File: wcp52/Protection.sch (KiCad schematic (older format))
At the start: 14 parts

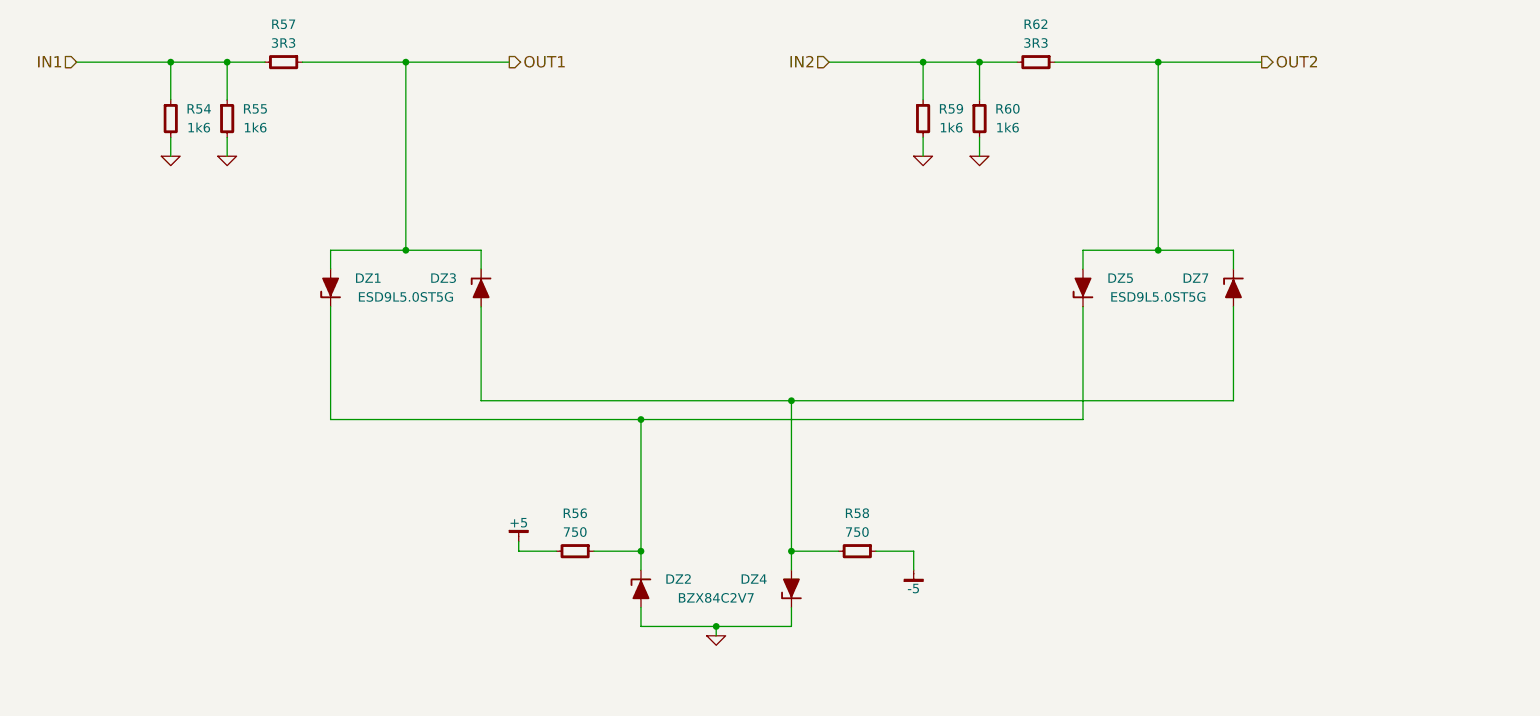
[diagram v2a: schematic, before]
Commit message: Reannotate parts. May need to tweak silkscreen
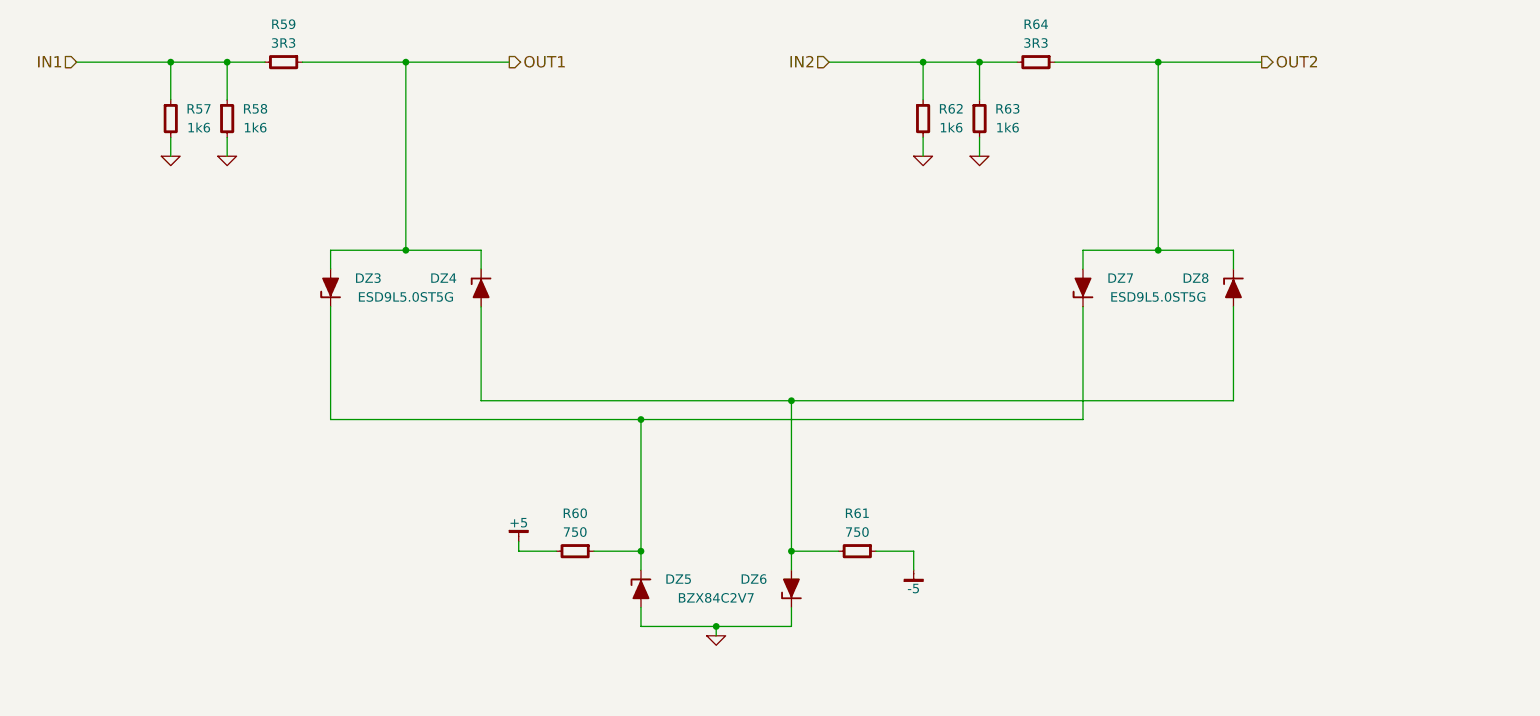
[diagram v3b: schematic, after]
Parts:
- DZ3: renamed from DZ1; OldReference (none) -> DZ1
- DZ4: renamed from DZ3; OldReference (none) -> DZ3
- DZ5: renamed from DZ2; OldReference (none) -> DZ2
- DZ6: renamed from DZ4; OldReference (none) -> DZ4
- DZ7: renamed from DZ5; OldReference (none) -> DZ5
- DZ8: renamed from DZ7; OldReference (none) -> DZ7
- R57: renamed from R54; OldReference (none) -> R54
- R58: renamed from R55; OldReference (none) -> R55
- R59: renamed from R57; OldReference (none) -> R57
- R60: renamed from R56; OldReference (none) -> R56
- R61: renamed from R58; OldReference (none) -> R58
- R62: renamed from R59; OldReference (none) -> R59
- R63: renamed from R60; OldReference (none) -> R60
- R64: renamed from R62; OldReference (none) -> R62
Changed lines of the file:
@@
 F 2 "" H 2900 2800 60  0000 C CNN
 F 3 "" H 2900 2800 60  0000 C CNN
+F 4 "#PWR0171" H 2900 2800 50  0001 C CNN "OldReference"
 	1    2900 2800
 	1    0    0    -1
@@
 F 2 "" H 3200 2800 60  0000 C CNN
 F 3 "" H 3200 2800 60  0000 C CNN
+F 4 "#PWR0172" H 3200 2800 50  0001 C CNN "OldReference"
 	1    3200 2800
 	1    0    0    -1
@@
 Connection ~ 3200 2300
 $Comp
-L ESD9L DZ1
+L ESD9L DZ3
 U 1 1 54F315E0
 P 3750 3500
-F 0 "DZ1" H 3950 3450 50  0000 C CNN
+F 0 "DZ3" H 3950 3450 50  0000 C CNN
 F 1 "ESD9L5.0ST5G" H 4150 3550 50  0000 C CNN
 F 2 "smd-semi:SOD-923" H 3750 3500 50  0001 C CNN
@@
 F 4 "Value" H 3750 3500 60  0001 C CNN "Manuf"
 F 5 "DIST DIGIKEY ESD9L5.0ST5GOSCT-ND" H 3750 3500 60  0001 C CNN "BOM"
+F 6 "DZ1" H 3750 3500 50  0001 C CNN "OldReference"
 	1    3750 3500
 	1    0    0    1
 $EndComp
 $Comp
-L ESD9L DZ3
+L ESD9L DZ4
 U 1 1 54F316A8
 P 4550 3500
-F 0 "DZ3" H 4350 3550 50  0000 C CNN
+F 0 "DZ4" H 4350 3550 50  0000 C CNN
 F 1 "ESD9L5.0ST5G" H 4950 3550 50  0001 C CNN
 F 2 "smd-semi:SOD-923" H 4550 3500 50  0001 C CNN
@@
 F 5 "ONSemi" H 4550 3500 60  0001 C CNN "Manuf"
 F 6 "DIST DIGIKEY ESD9L5.0ST5GOSCT-ND" H 4550 3500 60  0001 C CNN "BOM"
+F 7 "DZ3" H 4550 3500 50  0001 C CNN "OldReference"
 	1    4550 3500
 	1    0    0    -1
 $EndComp
 $Comp
-L BZX84 DZ2
+L BZX84 DZ5
 U 1 1 54F319D0
 P 5400 5100
-F 0 "DZ2" H 5600 5150 50  0000 C CNN
+F 0 "DZ5" H 5600 5150 50  0000 C CNN
 F 1 "BZX84C2V7" H 5800 5050 50  0000 C CNN
 F 2 "smd-semi:SOT-23" H 5400 5100 50  0001 C CNN
@@
 F 5 "ONSemi" H 5400 5100 60  0001 C CNN "Manuf"
 F 6 "DIST DIGIKEY BZX84C2V7LT1GOSCT-ND" H 5400 5100 60  0001 C CNN "BOM"
+F 7 "DZ2" H 5400 5100 50  0001 C CNN "OldReference"
 	1    5400 5100
 	1    0    0    -1
 $EndComp
 $Comp
-L BZX84 DZ4
+L BZX84 DZ6
 U 1 1 54F321AA
 P 6200 5100
-F 0 "DZ4" H 6000 5050 50  0000 C CNN
+F 0 "DZ6" H 6000 5050 50  0000 C CNN
 F 1 "BZX84C2V7" H 6600 5050 50  0001 C CNN
 F 2 "smd-semi:SOT-23" H 6200 5100 50  0001 C CNN
@@
 F 5 "ONSemi" H 6200 5100 60  0001 C CNN "Manuf"
 F 6 "DIST DIGIKEY BZX84C2V7LT1GOSCT-ND" H 6200 5100 60  0001 C CNN "BOM"
+F 7 "DZ4" H 6200 5100 50  0001 C CNN "OldReference"
 	1    6200 5100
 	1    0    0    1
@@
 F 2 "" H 5800 5350 60  0000 C CNN
 F 3 "" H 5800 5350 60  0000 C CNN
+F 4 "#PWR0173" H 5800 5350 50  0001 C CNN "OldReference"
 	1    5800 5350
 	1    0    0    -1
@@
 F 2 "" H 4750 4850 60  0000 C CNN
 F 3 "" H 4750 4850 60  0000 C CNN
+F 4 "#PWR0174" H 4750 4850 50  0001 C CNN "OldReference"
 	1    4750 4850
 	1    0    0    -1
@@
 F 2 "" H 6850 5000 60  0000 C CNN
 F 3 "" H 6850 5000 60  0000 C CNN
+F 4 "#PWR0175" H 6850 5000 50  0001 C CNN "OldReference"
 	1    6850 5000
 	1    0    0    -1
@@
 F 2 "" H 6900 2800 60  0000 C CNN
 F 3 "" H 6900 2800 60  0000 C CNN
+F 4 "#PWR0176" H 6900 2800 50  0001 C CNN "OldReference"
 	1    6900 2800
 	1    0    0    -1
@@
 F 2 "" H 7200 2800 60  0000 C CNN
 F 3 "" H 7200 2800 60  0000 C CNN
+F 4 "#PWR0177" H 7200 2800 50  0001 C CNN "OldReference"
 	1    7200 2800
 	1    0    0    -1
@@
 Connection ~ 7200 2300
 $Comp
-L ESD9L DZ5
+L ESD9L DZ7
 U 1 1 54F32C26
 P 7750 3500
-F 0 "DZ5" H 7950 3450 50  0000 C CNN
+F 0 "DZ7" H 7950 3450 50  0000 C CNN
 F 1 "ESD9L5.0ST5G" H 8150 3550 50  0000 C CNN
 F 2 "smd-semi:SOD-923" H 7750 3500 50  0001 C CNN
@@
 F 4 "Value" H 7750 3500 60  0001 C CNN "Manuf"
 F 5 "DIST DIGIKEY ESD9L5.0ST5GOSCT-ND" H 7750 3500 60  0001 C CNN "BOM"
+F 6 "DZ5" H 7750 3500 50  0001 C CNN "OldReference"
 	1    7750 3500
 	1    0    0    1
 $EndComp
 $Comp
-L ESD9L DZ7
+L ESD9L DZ8
 U 1 1 54F32C2F
 P 8550 3500
-F 0 "DZ7" H 8350 3550 50  0000 C CNN
+F 0 "DZ8" H 8350 3550 50  0000 C CNN
 F 1 "ESD9L5.0ST5G" H 8950 3550 50  0001 C CNN
 F 2 "smd-semi:SOD-923" H 8550 3500 50  0001 C CNN
@@
 F 5 "ONSemi" H 8550 3500 60  0001 C CNN "Manuf"
 F 6 "DIST DIGIKEY ESD9L5.0ST5GOSCT-ND" H 8550 3500 60  0001 C CNN "BOM"
+F 7 "DZ7" H 8550 3500 50  0001 C CNN "OldReference"
 	1    8550 3500
 	1    0    0    -1
@@
 Connection ~ 6200 4100
 $Comp
-L R-0603 R54
+L R-0603 R57
 U 1 1 5503F4A5
 P 2900 2600
-F 0 "R54" H 3050 2650 50  0000 C CNN
+F 0 "R57" H 3050 2650 50  0000 C CNN
 F 1 "1k6" H 3050 2550 50  0000 C CNN
 F 2 "IPC7351-Nominal:RESC1608X50" H 2900 2600 50  0001 C CNN
@@
 F 4 "Value" H 2900 2600 60  0001 C CNN "Manuf"
 F 5 "RES SMD 1.6k 1% [0603]" H 3650 3150 60  0001 C CNN "BOM"
+F 6 "R54" H 2900 2600 50  0001 C CNN "OldReference"
 	1    2900 2600
 	1    0    0    -1
 $EndComp
 $Comp
-L R-0603 R55
+L R-0603 R58
 U 1 1 5503F6C4
 P 3200 2600
-F 0 "R55" H 3350 2650 50  0000 C CNN
+F 0 "R58" H 3350 2650 50  0000 C CNN
 F 1 "1k6" H 3350 2550 50  0000 C CNN
 F 2 "IPC7351-Nominal:RESC1608X50" H 3200 2600 50  0001 C CNN
@@
 F 4 "Value" H 3200 2600 60  0001 C CNN "Manuf"
 F 5 "RES SMD 1.6k 1% [0603]" H 3950 3150 60  0001 C CNN "BOM"
+F 6 "R55" H 3200 2600 50  0001 C CNN "OldReference"
 	1    3200 2600
 	1    0    0    -1
 $EndComp
 $Comp
-L R-0603 R59
+L R-0603 R62
 U 1 1 5503F702
 P 6900 2600
-F 0 "R59" H 7050 2650 50  0000 C CNN
+F 0 "R62" H 7050 2650 50  0000 C CNN
 F 1 "1k6" H 7050 2550 50  0000 C CNN
 F 2 "IPC7351-Nominal:RESC1608X50" H 6900 2600 50  0001 C CNN
@@
 F 4 "Value" H 6900 2600 60  0001 C CNN "Manuf"
 F 5 "RES SMD 1.6k 1% [0603]" H 7650 3150 60  0001 C CNN "BOM"
+F 6 "R59" H 6900 2600 50  0001 C CNN "OldReference"
 	1    6900 2600
 	1    0    0    -1
 $EndComp
 $Comp
-L R-0603 R60
+L R-0603 R63
 U 1 1 5503F89E
 P 7200 2600
-F 0 "R60" H 7350 2650 50  0000 C CNN
+F 0 "R63" H 7350 2650 50  0000 C CNN
 F 1 "1k6" H 7350 2550 50  0000 C CNN
 F 2 "IPC7351-Nominal:RESC1608X50" H 7200 2600 50  0001 C CNN
@@
 F 4 "Value" H 7200 2600 60  0001 C CNN "Manuf"
 F 5 "RES SMD 1.6k 1% [0603]" H 7950 3150 60  0001 C CNN "BOM"
+F 6 "R60" H 7200 2600 50  0001 C CNN "OldReference"
 	1    7200 2600
 	1    0    0    -1
 $EndComp
 $Comp
-L R-0603 R57
+L R-0603 R59
 U 1 1 55041575
 P 3500 2300
-F 0 "R57" V 3300 2300 50  0000 C CNN
+F 0 "R59" V 3300 2300 50  0000 C CNN
 F 1 "3R3" V 3400 2300 50  0000 C CNN
 F 2 "IPC7351-Nominal:RESC1608X50" H 3500 2300 50  0001 C CNN
@@
 F 4 "Value" H 3500 2300 60  0001 C CNN "Manuf"
 F 5 "RES SMD 3.3 5% [0603]" H 4250 2850 60  0001 C CNN "BOM"
+F 6 "R57" H 3500 2300 50  0001 C CNN "OldReference"
 	1    3500 2300
 	0    1    1    0
 $EndComp
 $Comp
-L R-0603 R62
+L R-0603 R64
 U 1 1 5504172F
 P 7500 2300
-F 0 "R62" V 7300 2300 50  0000 C CNN
+F 0 "R64" V 7300 2300 50  0000 C CNN
 F 1 "3R3" V 7400 2300 50  0000 C CNN
 F 2 "IPC7351-Nominal:RESC1608X50" H 7500 2300 50  0001 C CNN
@@
 F 4 "Value" H 7500 2300 60  0001 C CNN "Manuf"
 F 5 "RES SMD 3.3 5% [0603]" H 8250 2850 60  0001 C CNN "BOM"
+F 6 "R62" H 7500 2300 50  0001 C CNN "OldReference"
 	1    7500 2300
 	0    1    1    0
 $EndComp
 $Comp
-L R-0603 R56
+L R-0603 R60
 U 1 1 54FE871D
 P 5050 4900
-F 0 "R56" V 4850 4900 50  0000 C CNN
+F 0 "R60" V 4850 4900 50  0000 C CNN
 F 1 "750" V 4950 4900 50  0000 C CNN
 F 2 "IPC7351-Nominal:RESC1608X50" H 5050 4900 50  0001 C CNN
@@
 F 4 "Value" H 5050 4900 60  0001 C CNN "Manuf"
 F 5 "RES SMD 750 1% [0603]" H 5800 5450 60  0001 C CNN "BOM"
+F 6 "R56" H 5050 4900 50  0001 C CNN "OldReference"
 	1    5050 4900
 	0    1    1    0
 $EndComp
 $Comp
-L R-0603 R58
+L R-0603 R61
 U 1 1 54FE88AB
 P 6550 4900
-F 0 "R58" V 6350 4900 50  0000 C CNN
+F 0 "R61" V 6350 4900 50  0000 C CNN
 F 1 "750" V 6450 4900 50  0000 C CNN
 F 2 "IPC7351-Nominal:RESC1608X50" H 6550 4900 50  0001 C CNN
@@
 F 4 "Value" H 6550 4900 60  0001 C CNN "Manuf"
 F 5 "RES SMD 750 1% [0603]" H 7300 5450 60  0001 C CNN "BOM"
+F 6 "R58" H 6550 4900 50  0001 C CNN "OldReference"
 	1    6550 4900
 	0    1    1    0

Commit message: Schematic touchups
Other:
- moved on the sheet: DZ3, DZ4, DZ5, DZ6, DZ7, DZ8, R57, R58, R59, R60, R61, R62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

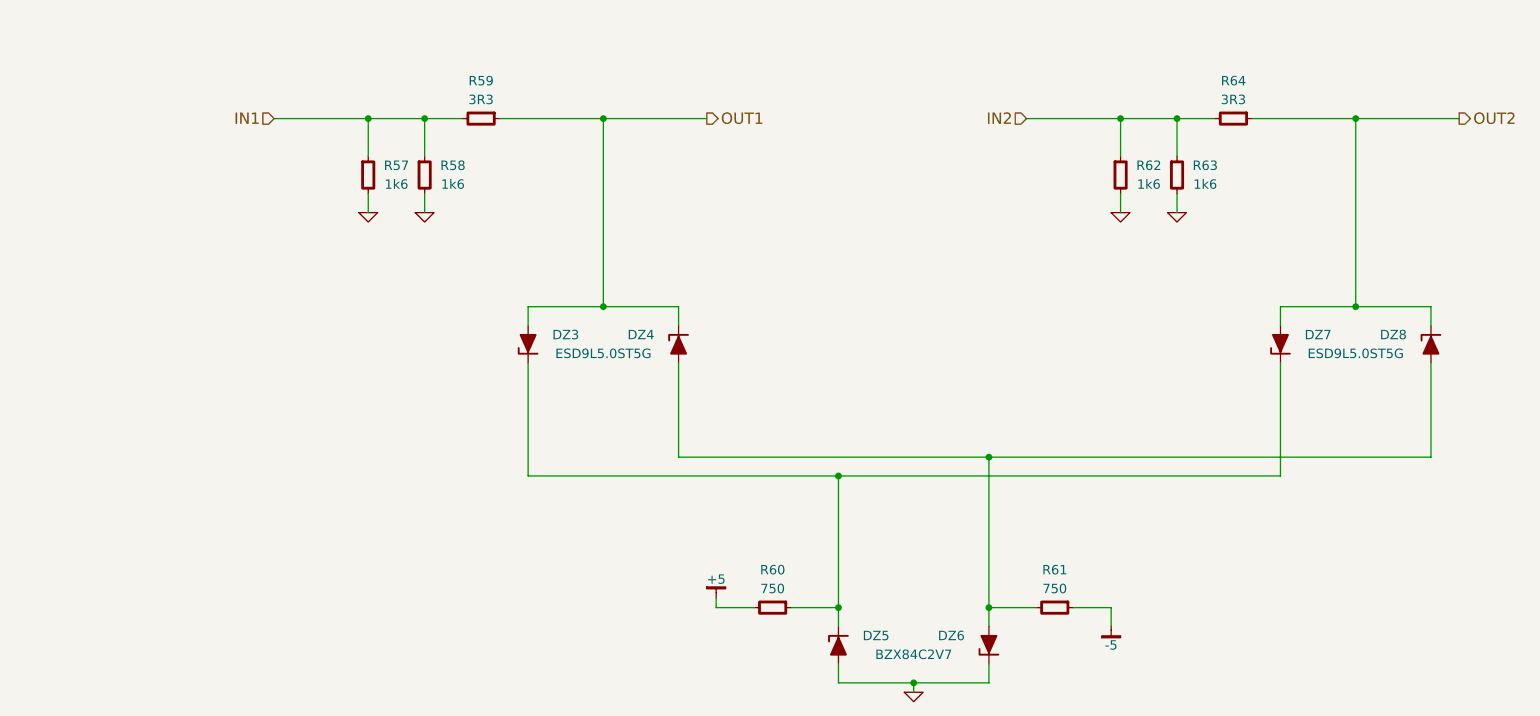
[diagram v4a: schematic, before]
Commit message: Change schematic pages to letter size
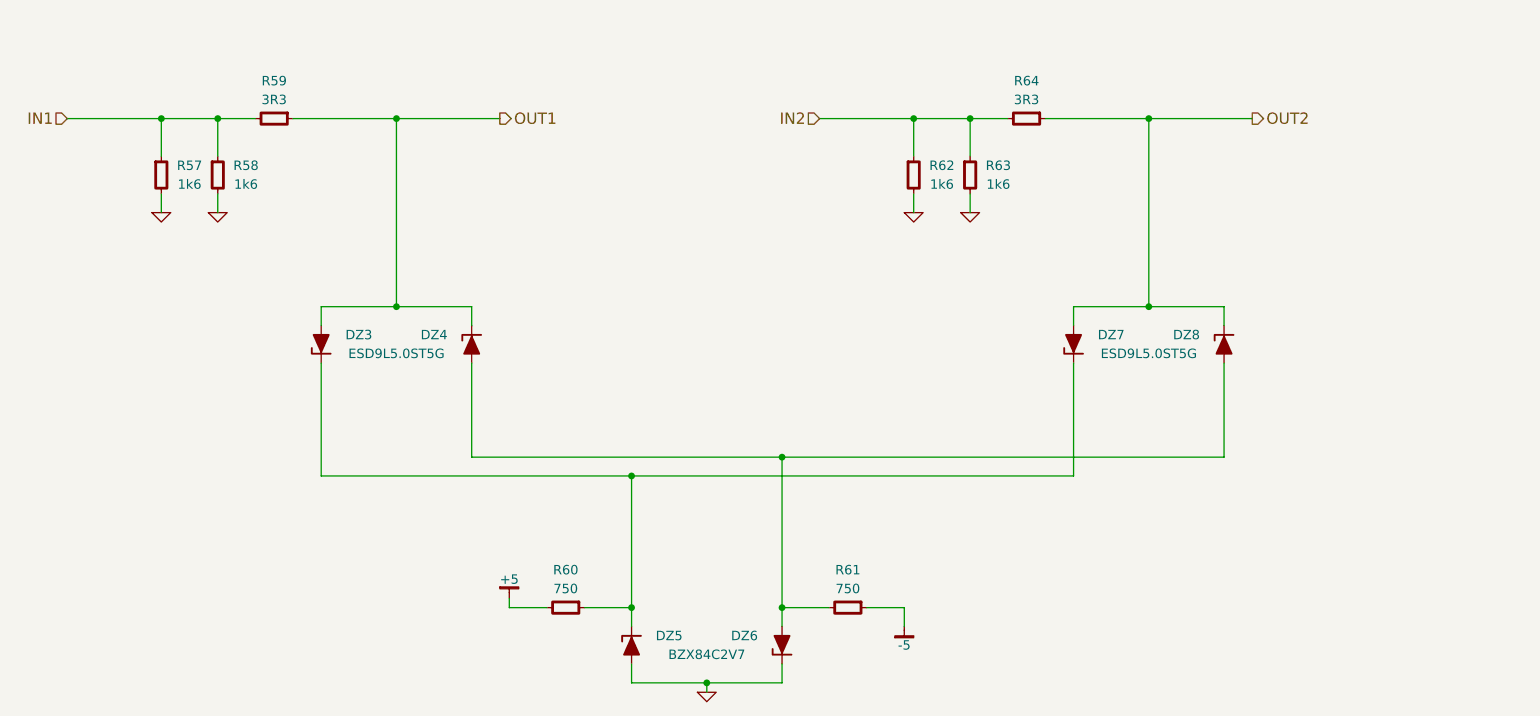
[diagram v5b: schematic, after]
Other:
- moved on the sheet: DZ3, DZ4, DZ5, DZ6, DZ7, DZ8, R57, R58, R59, R60, R61, R62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

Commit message: BOM fixes
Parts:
- DZ3, DZ7: BOM DIST DIGIKEY ESD9L5.0ST5GOSCT-ND -> SEMI ONSEMI ESD9L5.0ST5G; Manuf Value -> ONSemi; PN (none) -> ESD9L5.0ST5G
- DZ4, DZ8: BOM DIST DIGIKEY ESD9L5.0ST5GOSCT-ND -> SEMI ONSEMI ESD9L5.0ST5G
- DZ5, DZ6: BOM DIST DIGIKEY BZX84C2V7LT1GOSCT-ND -> SEMI GENERIC BZX84C2V7; Manuf ONSemi -> (none); PN BZX84C2V7LT1G -> BZX84C2V7
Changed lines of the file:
@@
 EESchema Schematic File Version 2
-LIBS:Altera
-LIBS:AnalogDevices
-LIBS:Atmel
-LIBS:conn-2mm
-LIBS:conn-100mil
-LIBS:conn-cui
-LIBS:conn-fci
-LIBS:conn-linx
-LIBS:conn-molex
-LIBS:conn-tagconnect
-LIBS:conn-test
-LIBS:DiodesInc
-LIBS:display
-LIBS:_electromech
-LIBS:Fairchild
-LIBS:FTDI
-LIBS:Intersil
-LIBS:Lattice
-LIBS:_linear
-LIBS:LinearTech
-LIBS:Littelfuse
-LIBS:logic-4000
-LIBS:logic-7400
-LIBS:MACOM
-LIBS:maxim
-LIBS:mechanical
-LIBS:Microchip
-LIBS:Micron
-LIBS:NXP
-LIBS:onsemi
-LIBS:passive
-LIBS:pasv-BiTech
-LIBS:pasv-Bourns
-LIBS:pasv-cap
-LIBS:pasv-ind
-LIBS:pasv-res
-LIBS:pcb
-LIBS:power
-LIBS:_semi
-LIBS:semi-diode-1N
-LIBS:semi-diode-BA
-LIBS:semi-diode-MCC
-LIBS:semi-diode-MMB
-LIBS:semi-diode-NXP
-LIBS:semi-diode-OnSemi
-LIBS:semi-diode-Vishay
-LIBS:semi-opto-misc
-LIBS:semi-thyristor-2N
-LIBS:semi-trans-2N
-LIBS:semi-trans-AO
-LIBS:semi-trans-BC
-LIBS:semi-trans-DiodesInc
-LIBS:semi-trans-Fairchild
-LIBS:semi-trans-Infineon
-LIBS:semi-trans-IntRect
-LIBS:semi-trans-IXYS
-LIBS:semi-trans-misc
-LIBS:semi-trans-MMB
-LIBS:semi-trans-MPS
-LIBS:semi-trans-NXP
-LIBS:semi-trans-PZT
-LIBS:semi-trans-TI
-LIBS:semi-trans-TIP
-LIBS:semi-trans-Toshiba
-LIBS:silabs
-LIBS:skyworks
-LIBS:ST
-LIBS:st_ic
-LIBS:st_semi
-LIBS:supertex
-LIBS:symbol
-LIBS:TexasInstruments
-LIBS:vishay_semi
-LIBS:Xilinx
-LIBS:pasv-xtal
-LIBS:conn-te
 LIBS:wcp52-cache
 EELAYER 25 0
@@
 F 2 "smd-semi:SOD-923" H 3700 3800 50  0001 C CNN
 F 3 "" H 3700 3800 60  0000 C CNN
-F 4 "Value" H 3700 3800 60  0001 C CNN "Manuf"
-F 5 "DIST DIGIKEY ESD9L5.0ST5GOSCT-ND" H 3700 3800 60  0001 C CNN "BOM"
-F 6 "DZ1" H 3700 3800 50  0001 C CNN "OldReference"
+F 4 "ESD9L5.0ST5G" H 3700 3800 60  0001 C CNN "PN"
+F 5 "ONSemi" H 3700 3800 60  0001 C CNN "Manuf"
+F 6 "SEMI ONSEMI ESD9L5.0ST5G" H 3700 3800 60  0001 C CNN "BOM"
+F 7 "DZ1" H 3700 3800 50  0001 C CNN "OldReference"
 	1    3700 3800
 	1    0    0    1
@@
 F 4 "ESD9L5.0ST5G" H 4500 3800 60  0001 C CNN "PN"
 F 5 "ONSemi" H 4500 3800 60  0001 C CNN "Manuf"
-F 6 "DIST DIGIKEY ESD9L5.0ST5GOSCT-ND" H 4500 3800 60  0001 C CNN "BOM"
+F 6 "SEMI ONSEMI ESD9L5.0ST5G" H 4500 3800 60  0001 C CNN "BOM"
 F 7 "DZ3" H 4500 3800 50  0001 C CNN "OldReference"
 	1    4500 3800
@@
 F 2 "smd-semi:SOT-23" H 5350 5400 50  0001 C CNN
 F 3 "" H 5350 5400 60  0000 C CNN
-F 4 "BZX84C2V7LT1G" H 5350 5400 60  0001 C CNN "PN"
-F 5 "ONSemi" H 5350 5400 60  0001 C CNN "Manuf"
-F 6 "DIST DIGIKEY BZX84C2V7LT1GOSCT-ND" H 5350 5400 60  0001 C CNN "BOM"
-F 7 "DZ2" H 5350 5400 50  0001 C CNN "OldReference"
+F 4 "BZX84C2V7" H 5350 5400 60  0001 C CNN "PN"
+F 5 "SEMI GENERIC BZX84C2V7" H 5350 5400 60  0001 C CNN "BOM"
+F 6 "DZ2" H 5350 5400 50  0001 C CNN "OldReference"
 	1    5350 5400
 	1    0    0    -1
@@
 F 2 "smd-semi:SOT-23" H 6150 5400 50  0001 C CNN
 F 3 "" H 6150 5400 60  0000 C CNN
-F 4 "BZX84C2V7LT1G" H 6150 5400 60  0001 C CNN "PN"
-F 5 "ONSemi" H 6150 5400 60  0001 C CNN "Manuf"
-F 6 "DIST DIGIKEY BZX84C2V7LT1GOSCT-ND" H 6150 5400 60  0001 C CNN "BOM"
-F 7 "DZ4" H 6150 5400 50  0001 C CNN "OldReference"
+F 4 "BZX84C2V7" H 6150 5400 60  0001 C CNN "PN"
+F 5 "SEMI GENERIC BZX84C2V7" H 6150 5400 60  0001 C CNN "BOM"
+F 6 "DZ4" H 6150 5400 50  0001 C CNN "OldReference"
 	1    6150 5400
 	1    0    0    1
@@
 F 2 "smd-semi:SOD-923" H 7700 3800 50  0001 C CNN
 F 3 "" H 7700 3800 60  0000 C CNN
-F 4 "Value" H 7700 3800 60  0001 C CNN "Manuf"
-F 5 "DIST DIGIKEY ESD9L5.0ST5GOSCT-ND" H 7700 3800 60  0001 C CNN "BOM"
-F 6 "DZ5" H 7700 3800 50  0001 C CNN "OldReference"
+F 4 "ESD9L5.0ST5G" H 7700 3800 60  0001 C CNN "PN"
+F 5 "ONSemi" H 7700 3800 60  0001 C CNN "Manuf"
+F 6 "SEMI ONSEMI ESD9L5.0ST5G" H 7700 3800 60  0001 C CNN "BOM"
+F 7 "DZ5" H 7700 3800 50  0001 C CNN "OldReference"
 	1    7700 3800
 	1    0    0    1
@@
 F 4 "ESD9L5.0ST5G" H 8500 3800 60  0001 C CNN "PN"
 F 5 "ONSemi" H 8500 3800 60  0001 C CNN "Manuf"
-F 6 "DIST DIGIKEY ESD9L5.0ST5GOSCT-ND" H 8500 3800 60  0001 C CNN "BOM"
+F 6 "SEMI ONSEMI ESD9L5.0ST5G" H 8500 3800 60  0001 C CNN "BOM"
 F 7 "DZ7" H 8500 3800 50  0001 C CNN "OldReference"
 	1    8500 3800
